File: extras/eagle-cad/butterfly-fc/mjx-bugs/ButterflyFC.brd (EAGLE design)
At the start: 53.2 x 61 mm, 5 parts

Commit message: Added sodler pads
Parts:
- added PAD1, PAD10, PAD2, PAD3, PAD4, PAD5, PAD6, PAD7, PAD8, PAD9: (no value), wirepad:SMD2,54-5,08
- moved 5VREG 15.1 mm to (41.0, 11.0)
- moved J2 2.00 mm to (35.0, 57.5)
- moved J1 1.00 mm to (17.8, 24.5)
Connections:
- net GND: now also PAD10.1, PAD2.1, PAD4.1, PAD6.1, PAD8.1
- net VBAT: now also PAD1.1, PAD3.1, PAD5.1, PAD7.1, PAD9.1
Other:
- outline, holes or cut-outs redrawn

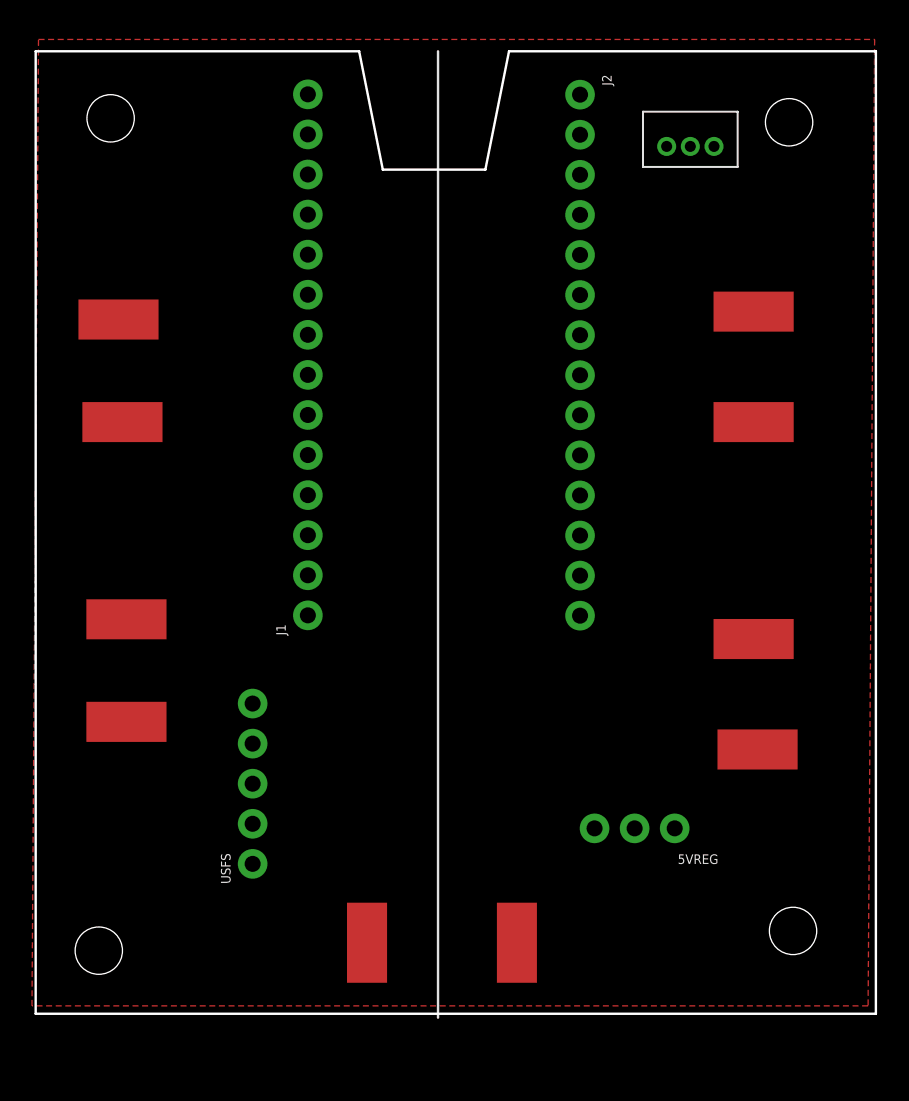
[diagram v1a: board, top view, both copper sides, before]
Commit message: Adjusted holes in board
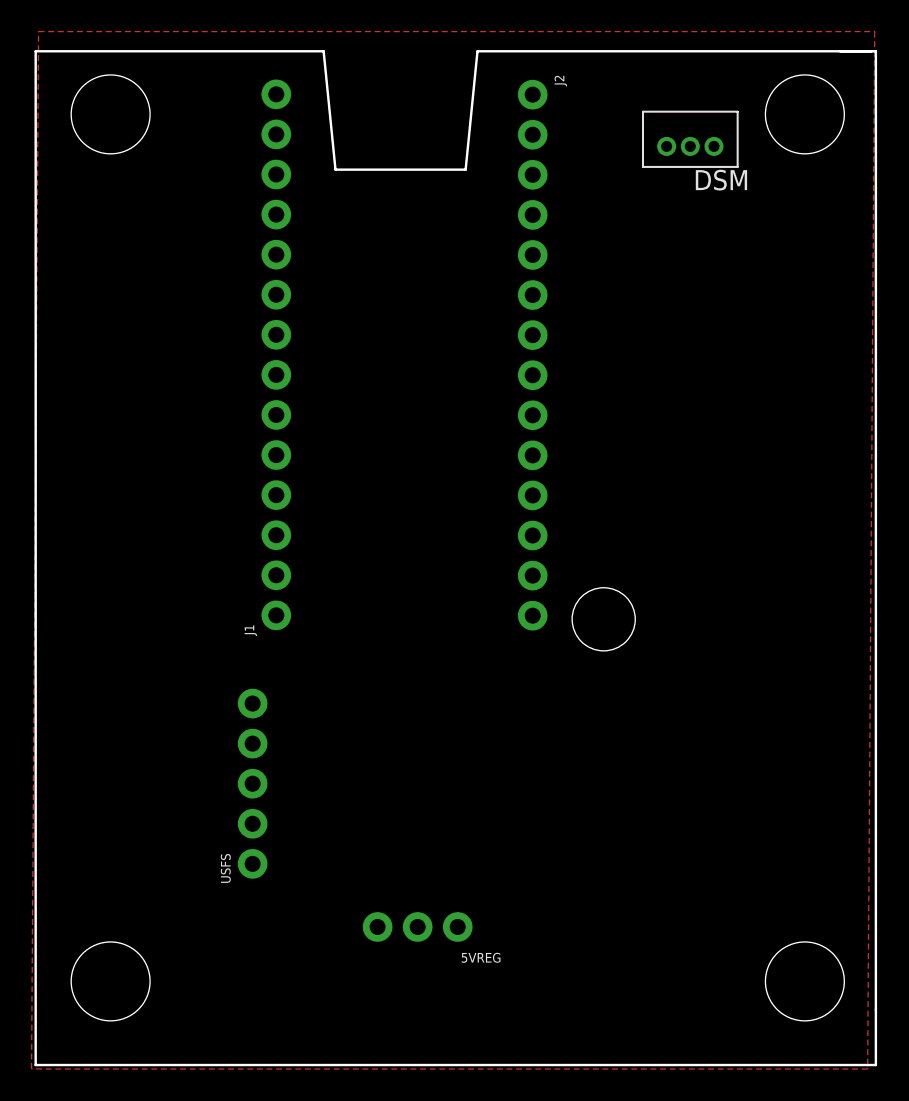
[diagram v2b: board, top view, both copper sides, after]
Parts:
- removed PAD1, PAD10, PAD2, PAD3, PAD4, PAD5, PAD6, PAD7, PAD8, PAD9: (no value), wirepad:SMD2,54-5,08
- moved 5VREG 15.1 mm to (27.2, 4.75)
- moved J2 3.00 mm to (32.0, 57.5)
- moved J1 2.00 mm to (15.8, 24.5)
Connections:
- net GND: no longer PAD10.1, PAD2.1, PAD4.1, PAD6.1, PAD8.1
- net VBAT: no longer PAD1.1, PAD3.1, PAD5.1, PAD7.1, PAD9.1
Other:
- board size 53.2 x 61 mm -> 53.2 x 64.2 mm

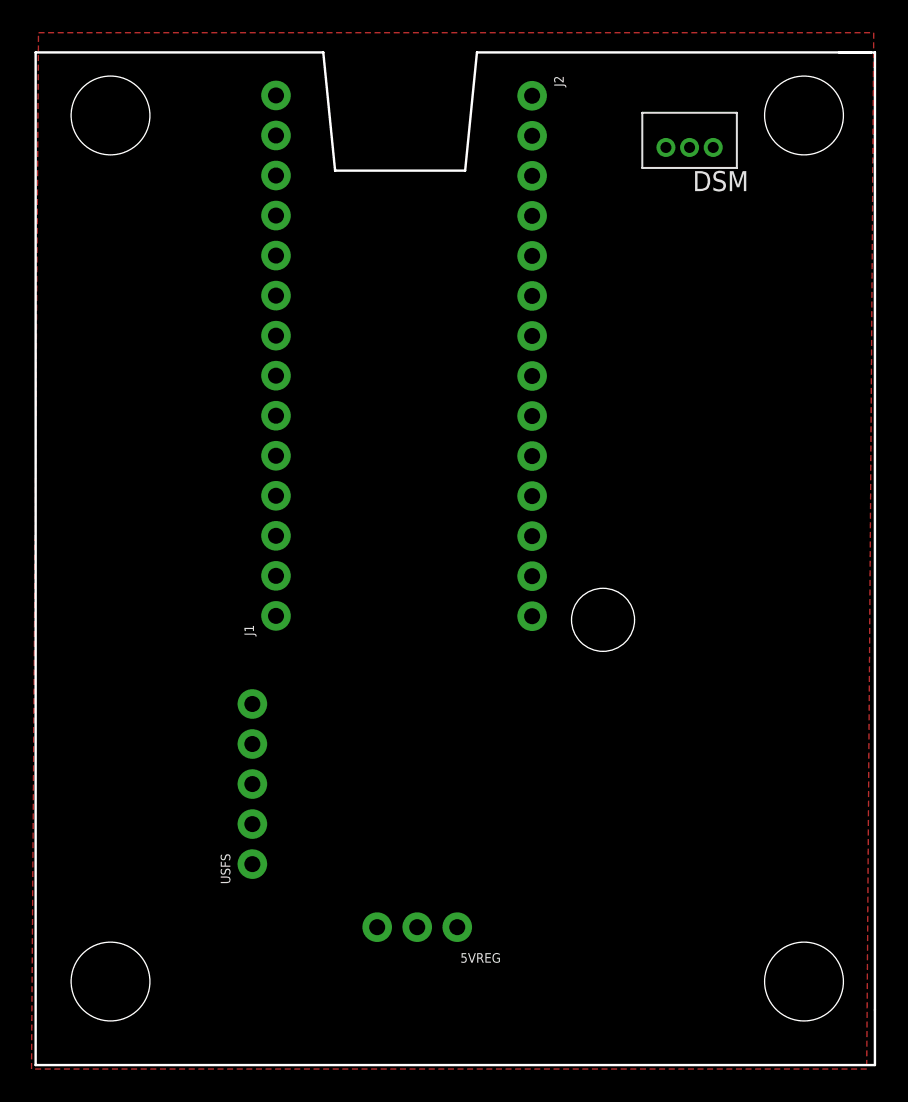
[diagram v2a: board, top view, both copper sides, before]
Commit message: Added solder pads
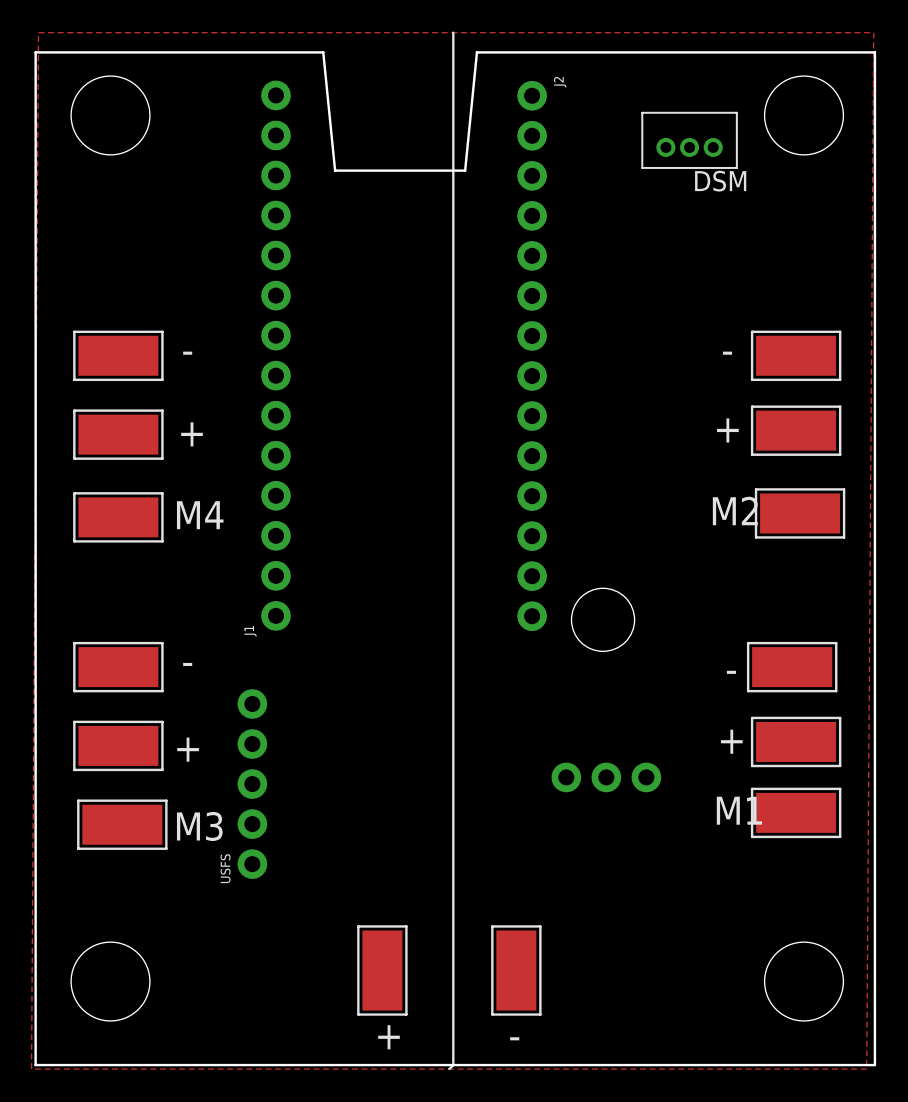
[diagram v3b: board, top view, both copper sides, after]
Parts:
- added PAD1, PAD10, PAD11, PAD12, PAD13, PAD14, PAD2, PAD3, PAD4, PAD5, PAD6, PAD7, PAD8, PAD9: WIREPADSMD5-2,5, wirepad:5-2,5
- moved 5VREG 15.3 mm to (39.2, 14.2)
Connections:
- new net M4: PAD12.1
- net GND: now also PAD10.1, PAD2.1, PAD4.1, PAD6.1, PAD8.1
- net M1: now also PAD13.1
- net M2: now also PAD14.1
- net M3: now also PAD11.1
- net VBAT: now also PAD1.1, PAD3.1, PAD5.1, PAD7.1, PAD9.1
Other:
- outline, holes or cut-outs redrawn
- board text added: "+"
- board text added: "-"
- board text added: "M1"
- board text added: "M2"
- board text added: "M3"
- board text added: "M4"
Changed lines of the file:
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@@
 <?xml version="1.0" encoding="utf-8"?>
 <!DOCTYPE eagle SYSTEM "eagle.dtd">
-<eagle version="9.1.1">
+<eagle version="9.6.2">
 <drawing>
 <settings>
@@
 <wire x1="19.5" y1="52.75" x2="27.75" y2="52.75" width="0.1524" layer="20"/>
 <wire x1="27.75" y1="52.75" x2="28.5" y2="60.25" width="0.1524" layer="20"/>
-<wire x1="28.5" y1="60.25" x2="51.5" y2="60.25" width="0.1524" layer="20"/>
-<wire x1="51.5" y1="60.25" x2="53.5" y2="60.25" width="0.1524" layer="20"/>
+<wire x1="28.5" y1="60.25" x2="53.75" y2="60.25" width="0.1524" layer="20"/>
 <wire x1="0.5" y1="60.25" x2="0.5" y2="-4" width="0.1524" layer="20"/>
 <wire x1="0.5" y1="-4" x2="53.75" y2="-4" width="0.1524" layer="20"/>
-<wire x1="53.75" y1="-4" x2="53.75" y2="-0.5" width="0.1524" layer="20"/>
-<wire x1="53.75" y1="-0.5" x2="53.75" y2="60.25" width="0.1524" layer="20"/>
-<wire x1="53.75" y1="60.25" x2="51.5" y2="60.25" width="0.1524" layer="20"/>
+<wire x1="53.75" y1="-4" x2="53.75" y2="60.25" width="0.1524" layer="20"/>
 <hole x="36.5" y="24.25" drill="4"/>
+<wire x1="27" y1="61.5" x2="27" y2="-4" width="0.1524" layer="21"/>
+<wire x1="27" y1="-4" x2="26.75" y2="-4.25" width="0.1524" layer="21"/>
+<text x="22" y="-3" size="1.778" layer="21">+</text>
+<text x="30.5" y="-3" size="1.778" layer="21">-</text>
+<text x="9.5" y="35.25" size="1.778" layer="21">+</text>
+<text x="9.25" y="15.25" size="1.778" layer="21">+</text>
+<text x="43.75" y="15.75" size="1.778" layer="21">+</text>
+<text x="43.5" y="35.5" size="1.778" layer="21">+</text>
+<text x="9.75" y="20.75" size="1.778" layer="21">-</text>
+<text x="9.75" y="40.5" size="1.778" layer="21">-</text>
+<text x="44" y="40.5" size="1.778" layer="21">-</text>
+<text x="44.25" y="20.25" size="1.778" layer="21">-</text>
+<text x="9.25" y="10.25" size="1.778" layer="21">M3</text>
+<text x="9.25" y="30" size="1.778" layer="21">M4</text>
+<text x="43.25" y="30.25" size="1.778" layer="21">M2</text>
+<text x="43.5" y="11.25" size="1.778" layer="21">M1</text>
 </plain>
 <attributes>
@@
 <attribute name="VALUE" x="29.968" y="58.77" size="0.6096" layer="27" font="vector" ratio="20" rot="R270"/>
 </element>
-<element name="5VREG" library="SparkFun-Connectors" package="1X03_NO_SILK" value="" x="27.25" y="4.75" smashed="yes" rot="R180">
-<attribute name="NAME" x="30.02" y="3.103" size="0.6096" layer="25" font="vector" ratio="20" rot="R180"/>
-<attribute name="VALUE" x="28.52" y="6.782" size="0.6096" layer="27" font="vector" ratio="20" rot="R180"/>
+<element name="5VREG" library="SparkFun-Connectors" package="1X03_NO_SILK" value="" x="39.25" y="14.25" smashed="yes" rot="R180">
+<attribute name="VALUE" x="40.52" y="16.282" size="0.6096" layer="27" font="vector" ratio="20" rot="R180"/>
 </element>
 <element name="USFS" library="SparkFun-Connectors" package="1X05_NO_SILK" value="" x="14.25" y="8.75" smashed="yes" rot="R90">
 <attribute name="NAME" x="12.853" y="7.48" size="0.6096" layer="25" font="vector" ratio="20" rot="R90"/>
 <attribute name="VALUE" x="16.282" y="7.48" size="0.6096" layer="27" font="vector" ratio="20" rot="R90"/>
+</element>
+<element name="PAD1" library="wirepad" package="5-2,5" value="WIREPADSMD5-2,5" x="22.5" y="2" smashed="yes">
+<attribute name="VALUE" x="22.4" y="4.8" size="0.0254" layer="27"/>
+</element>
+<element name="PAD2" library="wirepad" package="5-2,5" value="WIREPADSMD5-2,5" x="31" y="2" smashed="yes">
+<attribute name="VALUE" x="30.9" y="4.8" size="0.0254" layer="27"/>
+</element>
+<element name="PAD3" library="wirepad" package="5-2,5" value="WIREPADSMD5-2,5" x="5.75" y="36" smashed="yes" rot="R90">
+<attribute name="VALUE" x="2.95" y="35.9" size="0.0254" layer="27" rot="R90"/>
+</element>
+<element name="PAD4" library="wirepad" package="5-2,5" value="WIREPADSMD5-2,5" x="5.75" y="41" smashed="yes" rot="R90">
+<attribute name="VALUE" x="2.95" y="40.9" size="0.0254" layer="27" rot="R90"/>
+</element>
+<element name="PAD5" library="wirepad" package="5-2,5" value="WIREPADSMD5-2,5" x="5.75" y="16.25" smashed="yes" rot="R90">
+<attribute name="VALUE" x="2.95" y="16.15" size="0.0254" layer="27" rot="R90"/>
+</element>
+<element name="PAD6" library="wirepad" package="5-2,5" value="WIREPADSMD5-2,5" x="5.75" y="21.25" smashed="yes" rot="R90">
+<attribute name="VALUE" x="2.95" y="21.15" size="0.0254" layer="27" rot="R90"/>
+</element>
+<element name="PAD7" library="wirepad" package="5-2,5" value="WIREPADSMD5-2,5" x="48.75" y="16.5" smashed="yes" rot="R270">
+<attribute name="VALUE" x="51.55" y="16.6" size="0.0254" layer="27" rot="R270"/>
+</element>
+<element name="PAD8" library="wirepad" package="5-2,5" value="WIREPADSMD5-2,5" x="48.5" y="21.25" smashed="yes" rot="R90">
+<attribute name="VALUE" x="45.7" y="21.15" size="0.0254" layer="27" rot="R90"/>
+</element>
+<element name="PAD9" library="wirepad" package="5-2,5" value="WIREPADSMD5-2,5" x="48.75" y="36.25" smashed="yes" rot="R90">
+<attribute name="VALUE" x="45.95" y="36.15" size="0.0254" layer="27" rot="R90"/>
+</element>
+<element name="PAD10" library="wirepad" package="5-2,5" value="WIREPADSMD5-2,5" x="48.75" y="41" smashed="yes" rot="R90">
+<attribute name="VALUE" x="45.95" y="40.9" size="0.0254" layer="27" rot="R90"/>
+</element>
+<element name="PAD11" library="wirepad" package="5-2,5" value="WIREPADSMD5-2,5" x="6" y="11.25" smashed="yes" rot="R90">
+<attribute name="VALUE" x="3.2" y="11.15" size="0.0254" layer="27" rot="R90"/>
+</element>
+<element name="PAD12" library="wirepad" package="5-2,5" value="WIREPADSMD5-2,5" x="5.75" y="30.75" smashed="yes" rot="R90">
+<attribute name="VALUE" x="2.95" y="30.65" size="0.0254" layer="27" rot="R90"/>
+</element>
+<element name="PAD13" library="wirepad" package="5-2,5" value="WIREPADSMD5-2,5" x="48.75" y="12" smashed="yes" rot="R90">
+<attribute name="VALUE" x="45.95" y="11.9" size="0.0254" layer="27" rot="R90"/>
+</element>
+<element name="PAD14" library="wirepad" package="5-2,5" value="WIREPADSMD5-2,5" x="49" y="31" smashed="yes" rot="R90">
+<attribute name="VALUE" x="46.2" y="30.9" size="0.0254" layer="27" rot="R90"/>
 </element>
 </elements>
@@
 <contactref element="5VREG" pad="2"/>
 <contactref element="USFS" pad="5"/>
+<contactref element="PAD2" pad="1"/>
+<contactref element="PAD4" pad="1"/>
+<contactref element="PAD6" pad="1"/>
+<contactref element="PAD8" pad="1"/>
+<contactref element="PAD10" pad="1"/>
+<wire x1="32" y1="57.5" x2="41.99" y2="54.22" width="0" layer="19" extent="1-1"/>
+<wire x1="48.75" y1="41" x2="41.99" y2="54.22" width="0" layer="19" extent="1-1"/>
+<wire x1="48.5" y1="21.25" x2="48.75" y2="41" width="0" layer="19" extent="1-1"/>
+<wire x1="36.71" y1="14.25" x2="48.5" y2="21.25" width="0" layer="19" extent="1-1"/>
+<wire x1="31" y1="2" x2="36.71" y2="14.25" width="0" layer="19" extent="1-1"/>
+<wire x1="14.25" y1="18.91" x2="31" y2="2" width="0" layer="19" extent="1-1"/>
+<wire x1="15.75" y1="27.04" x2="14.25" y2="18.91" width="0" layer="19" extent="1-1"/>
+<wire x1="5.75" y1="21.25" x2="14.25" y2="18.91" width="0" layer="19" extent="1-1"/>
+<wire x1="5.75" y1="41" x2="15.75" y2="27.04" width="0" layer="19" extent="1-1"/>
 </signal>
 <signal name="5V">
 <contactref element="J1" pad="1"/>
 <contactref element="5VREG" pad="1"/>
-<wire x1="27.25" y1="4.75" x2="15.75" y2="24.5" width="0" layer="19" extent="1-1"/>
+<wire x1="39.25" y1="14.25" x2="15.75" y2="24.5" width="0" layer="19" extent="1-1"/>
 </signal>
 <signal name="3V3">
@@
 <signal name="M1">
 <contactref element="J2" pad="5"/>
+<contactref element="PAD13" pad="1"/>
+<wire x1="48.75" y1="12" x2="32" y2="47.34" width="0" layer="19" extent="1-1"/>
 </signal>
 <signal name="M2">
 <contactref element="J2" pad="6"/>
+<contactref element="PAD14" pad="1"/>
+<wire x1="32" y1="44.8" x2="49" y2="31" width="0" layer="19" extent="1-1"/>
 </signal>
 <signal name="M3">
 <contactref element="J2" pad="7"/>
+<contactref element="PAD11" pad="1"/>
+<wire x1="6" y1="11.25" x2="32" y2="42.26" width="0" layer="19" extent="1-1"/>
 </signal>
 <signal name="SCL">
@@
 <signal name="VBAT">
 <contactref element="5VREG" pad="3"/>
+<contactref element="PAD1" pad="1"/>
+<contactref element="PAD3" pad="1"/>
+<contactref element="PAD5" pad="1"/>
+<contactref element="PAD7" pad="1"/>
+<contactref element="PAD9" pad="1"/>
+<wire x1="48.75" y1="16.5" x2="48.75" y2="36.25" width="0" layer="19" extent="1-1"/>
+<wire x1="34.17" y1="14.25" x2="48.75" y2="16.5" width="0" layer="19" extent="1-1"/>
+<wire x1="22.5" y1="2" x2="34.17" y2="14.25" width="0" layer="19" extent="1-1"/>
+<wire x1="5.75" y1="16.25" x2="22.5" y2="2" width="0" layer="19" extent="1-1"/>
+<wire x1="5.75" y1="36" x2="5.75" y2="16.25" width="0" layer="19" extent="1-1"/>
+</signal>
+<signal name="M4">
+<contactref element="PAD12" pad="1"/>
 </signal>
 </signals>

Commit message: More ButterflyFC work
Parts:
- removed J1, J2: (no value), SparkFun-Connectors:1X14_NO_SILK
- added BLUE: (no value), SparkFun-Connectors:1X04_NO_SILK
- added MCU1, MCU2: (no value), SparkFun-Connectors:1X14_NO_SILK
- moved DSM 38.1 mm to (4.49, 47.5)
- moved 5VREG 11.8 mm to (36.8, 2.75), turned to 0 degrees
- moved USFS 3.00 mm to (11.2, 8.75)
- moved PAD2 2.14 mm to (31.8, 0.00)
- moved PAD1 1.77 mm to (22.2, 0.25)
- moved PAD11 1.58 mm to (4.50, 11.8)
- moved PAD12 1.58 mm to (4.25, 30.2)
- moved PAD3 1.50 mm to (4.25, 36.0)
- moved PAD4 1.50 mm to (4.25, 41.0)
- moved PAD6 1.50 mm to (4.25, 21.2)
- moved PAD8 1.50 mm to (50.0, 21.2)
- moved PAD10 1.25 mm to (50.0, 41.0)
- moved PAD13 1.25 mm to (50.0, 12.0)
- moved PAD14 1.25 mm to (50.2, 31.0)
- moved PAD5 1.25 mm to (4.50, 16.2)
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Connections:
- removed net RX: DSM.3, J2.2
- new net BLRX: BLUE.1
- new net BLTX: BLUE.2
- new net DSMX: DSM.3, MCU2.2
- net 3V3: now also BLUE.4, MCU1.3; no longer J1.3
- net 5V: now also MCU1.1; no longer J1.1
- net GND: now also BLUE.3, MCU1.2, MCU2.1; no longer J1.2, J2.1
- net M1: now also MCU2.5; no longer J2.5
- net M2: now also MCU2.6; no longer J2.6
- net M3: now also MCU2.7; no longer J2.7
- net SCL: now also MCU2.8; no longer J2.8
- net SDA: now also MCU2.9; no longer J2.9
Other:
- outline, holes or cut-outs redrawn
